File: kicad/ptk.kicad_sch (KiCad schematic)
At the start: 25 parts, among them J0 nice!view, U0 ProMicro-kbd

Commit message: add'l routing
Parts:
- removed H4: MountingHole_Pad, MountingHole:MountingHole_2.2mm_M2_Pad_Via, symbol Mechanical:MountingHole_Pad
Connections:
- net s0: now also U0.18 (F6); no longer U0.17 (F7)
- net s1: now also U0.7 (D4); no longer U0.18 (F6)
- net s10: now also U0.9 (D7); no longer U0.14 (B2)
- net s11: now also U0.17 (F7); no longer U0.15 (B3)
- net s12: now also U0.8 (C6); no longer U0.16 (B1)
- net s18: now also U0.14 (B2); no longer U0.8 (C6)
- net s19: now also U0.10 (E6); no longer U0.9 (D7)
- net s20: now also U0.15 (B3); no longer U0.10 (E6)
- net s8: now also U0.13 (B6); no longer U0.7 (D4)
- net s9: now also U0.16 (B1); no longer U0.13 (B6)
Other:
- moved on the sheet: H0, H1, H2, H3

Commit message: added boxes around the keys on the schematic because I'm weird like that
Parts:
- removed 10/19: keyswitch, chelming-kbd:choc_v1_hotswap_reversible, symbol Switch:SW_Push
- added 8/17: keyswitch, chelming-kbd:choc_v1_hotswap_reversible, symbol Switch:SW_Push
- U0: footprint chelming-kbd:ProMicro_v3_nice_view_reversible -> chelming-kbd:ProMicro_v3_nice!view_reversible
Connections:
- net GND: now also 8/17.1
- net s8: now also 8/17.2
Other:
- moved on the sheet: 0/9, 1/8, 12/17, 13/16, 14/15, 2/7, 21/24, 22/23, 27/28, 3/6, Bat+0, Bat-0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

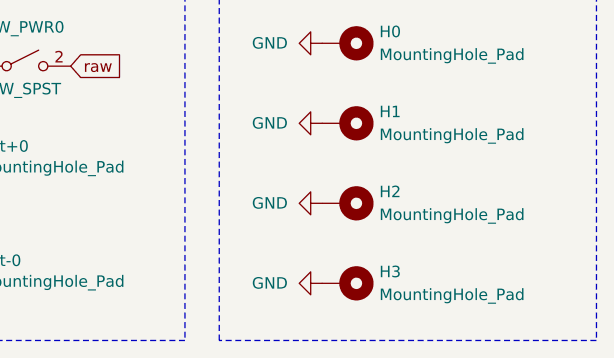
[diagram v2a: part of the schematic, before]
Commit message: removing mounting hole
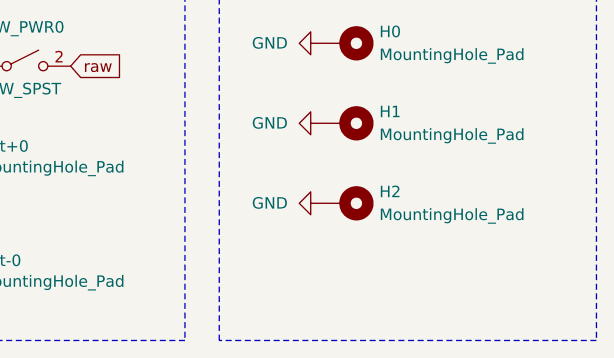
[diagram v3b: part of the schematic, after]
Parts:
- removed H3: MountingHole_Pad, MountingHole:MountingHole_2.2mm_M2_Pad_Via, symbol Mechanical:MountingHole_Pad
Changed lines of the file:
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@@
-	)
-	(symbol
-		(lib_name "MountingHole_Pad_1")
-		(lib_id "Mechanical:MountingHole_Pad")
-		(at 210.82 107.95 270)
-		(unit 1)
-		(exclude_from_sim yes)
-		(in_bom no)
-		(on_board yes)
-		(dnp no)
-		(fields_autoplaced yes)
-		(property "Reference" "H3"
-			(at 214.63 106.6799 90)
-			(effects
-				(font
-					(size 1.27 1.27)
-				)
-				(justify left)
-			)
-		)
-		(property "Value" "MountingHole_Pad"
-			(at 214.63 109.2199 90)
-			(effects
-				(font
-					(size 1.27 1.27)
-				)
-				(justify left)
-			)
-		)
-		(property "Footprint" "MountingHole:MountingHole_2.2mm_M2_Pad_Via"
-			(at 210.82 107.95 0)
-			(effects
-				(font
-					(size 1.27 1.27)
-				)
-				(hide yes)
-			)
-		)
-		(property "Datasheet" "~"
-			(at 210.82 107.95 0)
-			(effects
-				(font
-					(size 1.27 1.27)
-				)
-				(hide yes)
-			)
-		)
-		(property "Description" "Mounting Hole with connection"
-			(at 210.82 107.95 0)
-			(effects
-				(font
-					(size 1.27 1.27)
-				)
-				(hide yes)
-			)
-		)
-		(pin "1"
-		)
-		(instances
-			(project "reversiblepurringcat"
-				(path "/4e66a44f-7fa6-4e16-bf9b-62ec864301a5"
-					(reference "H3")
-					(unit 1)
-				)
-			)
-		)
 	)
 	(symbol
@@
 					(unit 1)
 				)
-			)
-		)
-	)
-	(symbol
-		(lib_id "power:GND")
-		(at 208.28 107.95 270)
-		(unit 1)
-		(exclude_from_sim no)
-		(in_bom yes)
-		(on_board yes)
-		(dnp no)
-		(fields_autoplaced yes)
-		(property "Reference" "#PWR09"
-			(at 201.93 107.95 0)
-			(effects
-				(font
-					(size 1.27 1.27)
-				)
-				(hide yes)
-			)
-		)
-		(property "Value" "GND"
-			(at 204.47 107.9499 90)
-			(effects
-				(font
-					(size 1.27 1.27)
-				)
-				(justify right)
-			)
-		)
-		(property "Footprint" ""
-			(at 208.28 107.95 0)
-			(effects
-				(font
-					(size 1.27 1.27)
-				)
-				(hide yes)
-			)
-		)
-		(property "Datasheet" ""
-			(at 208.28 107.95 0)
-			(effects
-				(font
-					(size 1.27 1.27)
-				)
-				(hide yes)
-			)
-		)
-		(property "Description" "Power symbol creates a global label with name \"GND\" , ground"
-			(at 208.28 107.95 0)
-			(effects
-				(font
-					(size 1.27 1.27)
-				)
-				(hide yes)
-			)
-		)
-		(pin "1"
-		)
-		(instances
-			(project ""
-				(path "/5bb59338-b7ae-4586-a4ee-509f5d9bc483"
-					(reference "#PWR09")
-					(unit 1)
-				)
